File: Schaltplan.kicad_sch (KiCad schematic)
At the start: 16 parts, among them K1 Relay, P1 USB Port vorheriger, P2 USB Port nächster, P4 USB Port Laden, U1 DC DC Wandler, U2 DC DC Wandler, U3 Digitaler Poti, U4 Display, U5 DC DC Wandler, U7 Digitaler Poti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

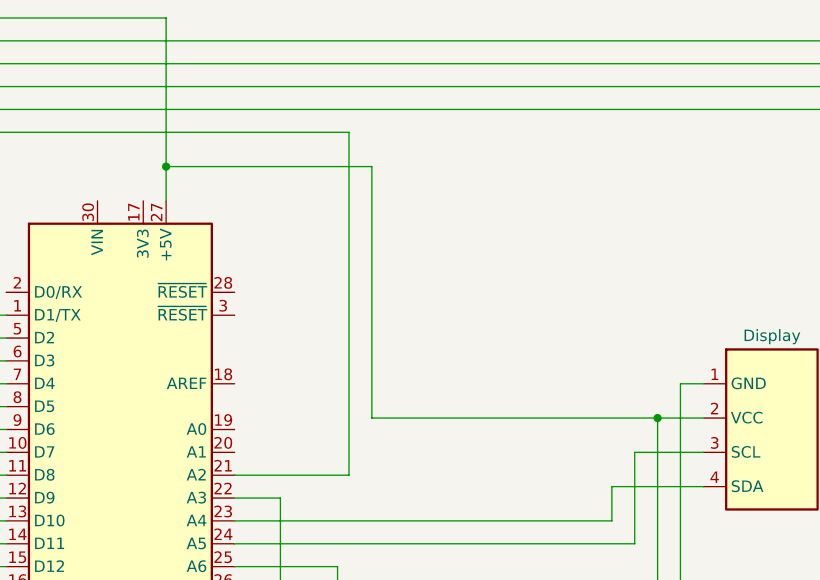
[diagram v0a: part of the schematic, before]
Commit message: Cables moved
Co-authored-by: JumpStone <hi@jumpstone4477.de>
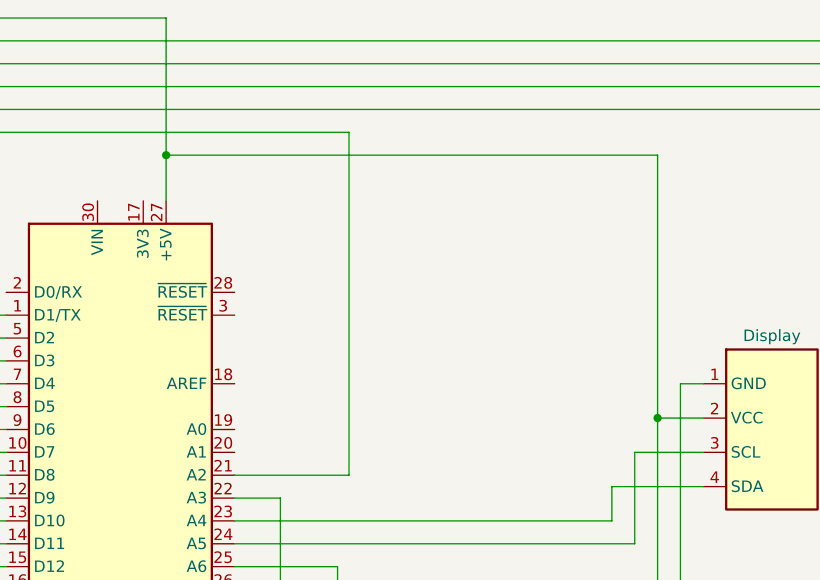
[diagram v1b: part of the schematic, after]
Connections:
- net at K1. (NC): now also A1.7 (D4)
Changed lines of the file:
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@@
+	)
+	(junction
+		(at 80.01 29.21)
+		(diameter 0)
+		(color 0 0 0 0)
 	)
 	(junction
@@
 	)
 	(junction
-		(at 80.01 30.48)
-		(diameter 0)
-		(color 0 0 0 0)
-	)
-	(junction
 		(at 57.15 130.81)
 		(diameter 0)
@@
 	(wire
 		(pts
-			(xy 80.01 30.48) (xy 80.01 34.29)
-		)
-		(stroke
-			(width 0)
-			(type default)
-		)
-	)
-	(wire
-		(pts
 			(xy 104.14 153.67) (xy 104.14 147.32)
 		)
@@
 	(wire
 		(pts
-			(xy 102.87 30.48) (xy 102.87 58.42)
+			(xy 134.62 29.21) (xy 134.62 58.42)
 		)
 		(stroke
@@
 	(wire
 		(pts
-			(xy 102.87 58.42) (xy 134.62 58.42)
-		)
-		(stroke
-			(width 0)
-			(type default)
-		)
-	)
-	(wire
-		(pts
 			(xy 123.19 105.41) (xy 123.19 95.25)
 		)
@@
 	(wire
 		(pts
-			(xy 102.87 30.48) (xy 80.01 30.48)
+			(xy 134.62 29.21) (xy 80.01 29.21)
 		)
 		(stroke
@@
 	(wire
 		(pts
-			(xy 80.01 13.97) (xy 80.01 30.48)
+			(xy 80.01 13.97) (xy 80.01 29.21)
 		)
 		(stroke
@@
 		)
 		(stroke
+			(width 0)
+			(type default)
+		)
+	)
+	(wire
+		(pts
+			(xy 80.01 29.21) (xy 80.01 34.29)
+		)
+		(stroke
